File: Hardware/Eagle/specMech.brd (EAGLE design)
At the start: 142.2 x 121.9 mm, 86 parts, among them J1 PINHD-1X8-MOLEX-SHROUD, J2 JST-2-PIN-2B-PH-K-S(LF)(SN), J3 PINHD-1X8-MOLEX-SHROUD, J4 PINHD-1X8-MOLEX-SHROUD, J6 Molex 0022232081, J7 Lantronix XPORT, J8 Molex 0022232081, U1 MCP23008-E/SO, U10 ADS1115, U11 MCP23008-E/SO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

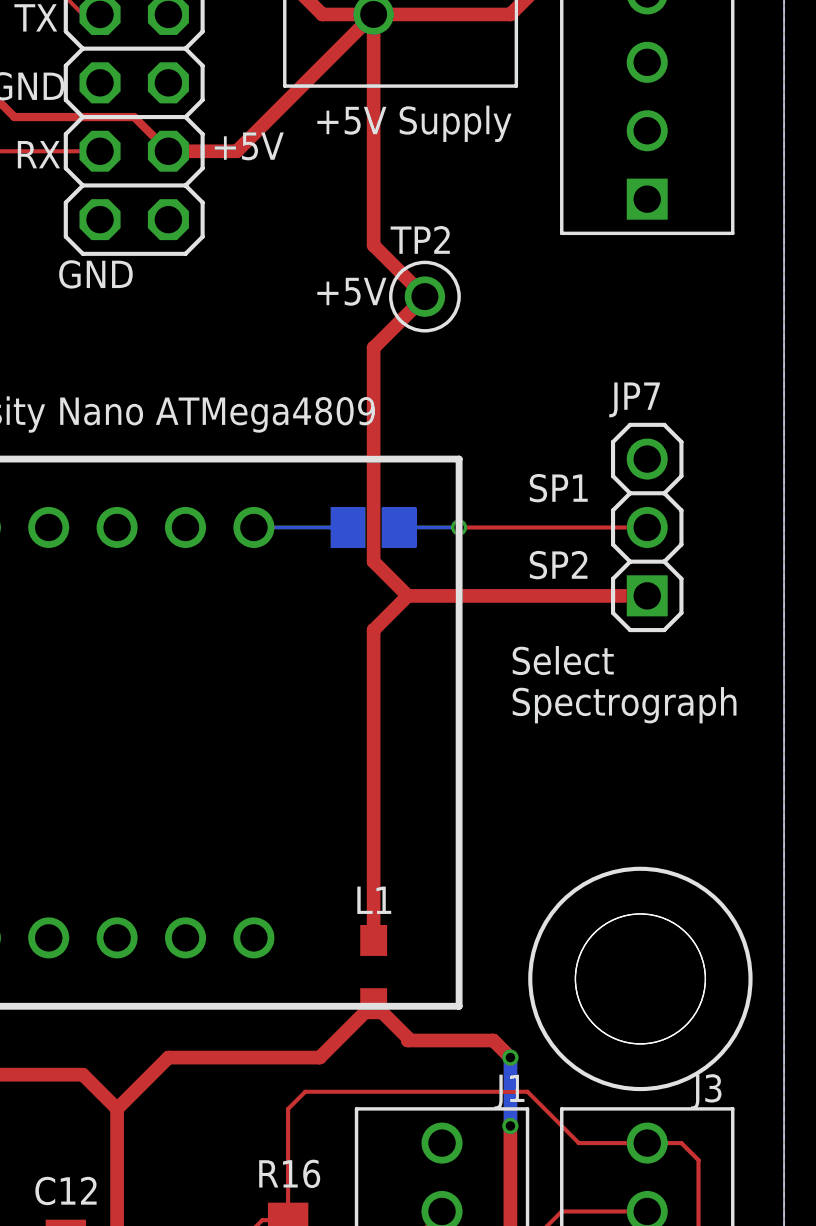
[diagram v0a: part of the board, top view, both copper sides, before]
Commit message: Starting major changes
Moved ferrite bead
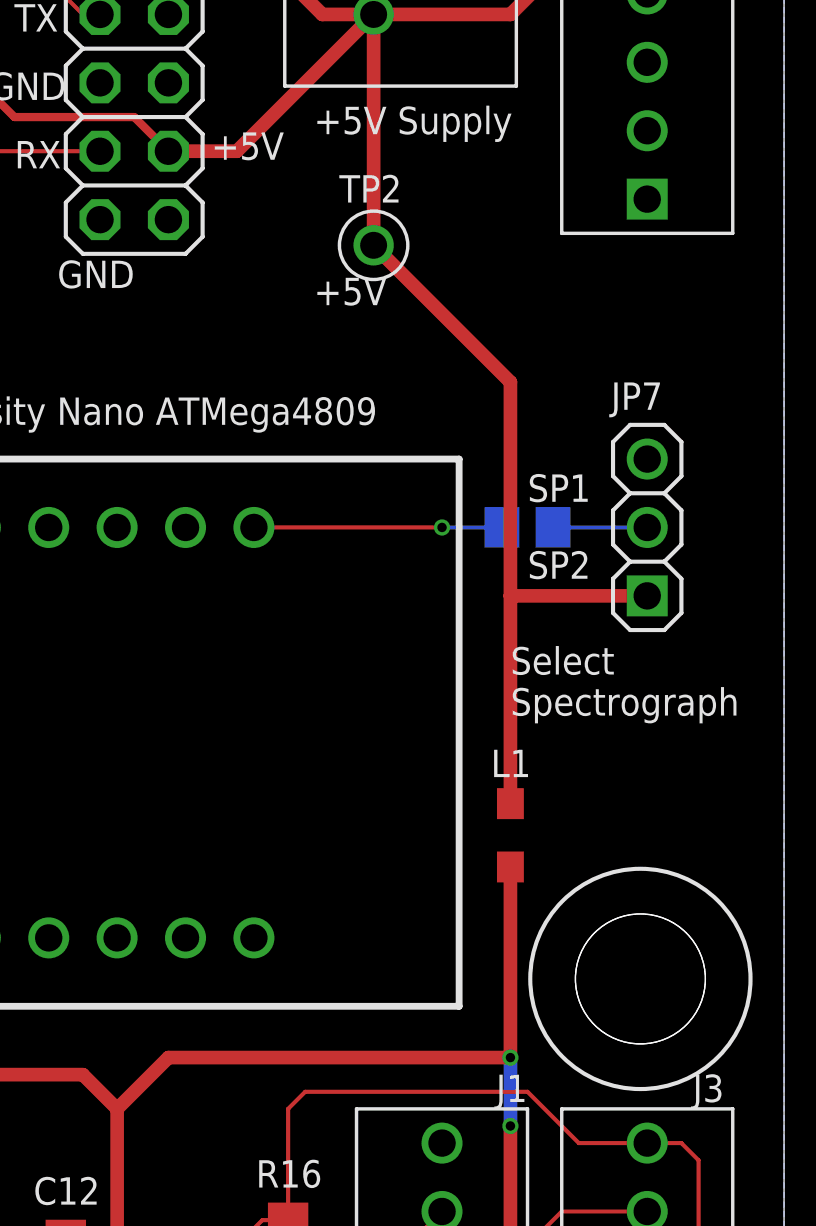
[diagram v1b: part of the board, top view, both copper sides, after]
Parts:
- moved L1 7.18 mm to (132.1, 55.9)
- moved R6 5.72 mm to (132.7, 67.3)
- moved TP2 2.69 mm to (127.0, 77.8)
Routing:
- net +5V: track 646.5 -> 637.1 mm
- net N$7: track 9.21 -> 3.50 mm, vias 1 -> 0
- net N$6: track 3.49 -> 9.21 mm, vias 0 -> 1
- net ADCVDD: track 132.5 -> 137.9 mm
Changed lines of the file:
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@@
 <attribute name="PURCHASE-URL" value="https://pricing.snapeda.com/search/part/EXB-38V103JV/?ref=eda" x="121.285" y="33.655" size="1.778" layer="27" display="off"/>
 </element>
-<element name="L1" library="AUmlib" library_urn="urn:adsk.eagle:library:9166017" package="INDC2012X87N" package3d_urn="urn:adsk.eagle:package:24287623/2" value="MMZ2012Y152BT000" x="127" y="50.8" smashed="yes" rot="R90">
-<attribute name="DESCRIPTION" value=" 1.5 kOhms @ 100MHz 1 Signal Line Ferrite Bead 0805 (2012 Metric) 500mA 400mOhm " x="127" y="50.8" size="1.778" layer="27" rot="R90" display="off"/>
-<attribute name="DIGI-KEY_PART_NUMBER" value="" x="127" y="50.8" size="1.778" layer="27" rot="R90" display="off"/>
-<attribute name="MF" value="TDK" x="127" y="50.8" size="1.778" layer="27" rot="R90" display="off"/>
-<attribute name="MP" value="MMZ2012Y152BT000" x="127" y="50.8" size="1.778" layer="27" rot="R90" display="off"/>
-<attribute name="NAME" x="127.768259375" y="53.975" size="1.016" layer="25" font="vector" rot="R180"/>
-<attribute name="PACKAGE" value="0805 TDK" x="127" y="50.8" size="1.778" layer="27" rot="R90" display="off"/>
-<attribute name="PURCHASE-URL" value="https://pricing.snapeda.com/search/part/MMZ2012Y152BT000/?ref=eda" x="127" y="50.8" size="1.778" layer="27" rot="R90" display="off"/>
+<element name="L1" library="AUmlib" library_urn="urn:adsk.eagle:library:9166017" package="INDC2012X87N" package3d_urn="urn:adsk.eagle:package:24287623/2" value="MMZ2012Y152BT000" x="132.08" y="55.88" smashed="yes" rot="R90">
+<attribute name="DESCRIPTION" value=" 1.5 kOhms @ 100MHz 1 Signal Line Ferrite Bead 0805 (2012 Metric) 500mA 400mOhm " x="132.08" y="55.88" size="1.778" layer="27" rot="R90" display="off"/>
+<attribute name="DIGI-KEY_PART_NUMBER" value="" x="132.08" y="55.88" size="1.778" layer="27" rot="R90" display="off"/>
+<attribute name="MF" value="TDK" x="132.08" y="55.88" size="1.778" layer="27" rot="R90" display="off"/>
+<attribute name="MP" value="MMZ2012Y152BT000" x="132.08" y="55.88" size="1.778" layer="27" rot="R90" display="off"/>
+<attribute name="NAME" x="132.848259375" y="59.055" size="1.016" layer="25" font="vector" rot="R180"/>
+<attribute name="PACKAGE" value="0805 TDK" x="132.08" y="55.88" size="1.778" layer="27" rot="R90" display="off"/>
+<attribute name="PURCHASE-URL" value="https://pricing.snapeda.com/search/part/MMZ2012Y152BT000/?ref=eda" x="132.08" y="55.88" size="1.778" layer="27" rot="R90" display="off"/>
 </element>
 <element name="C1" library="AUmlib" library_urn="urn:adsk.eagle:library:9166017" package="C0805" package3d_urn="urn:adsk.eagle:package:4021265/3" value="0.01uF" x="112.395" y="33.02" smashed="yes" rot="R270">
@@
 <attribute name="VALUE" x="140.335" y="63.5" size="1.27" layer="27" rot="R90"/>
 </element>
-<element name="R6" library="AUmlib" library_urn="urn:adsk.eagle:library:9166017" package="R0805" package3d_urn="urn:adsk.eagle:package:4021199/4" value="10K" x="127" y="67.31" smashed="yes" rot="MR180">
-<attribute name="NAME" x="126.365" y="69.85" size="1.016" layer="26" font="vector" rot="MR180"/>
-<attribute name="SPICEPREFIX" value="R" x="127" y="67.31" size="1.778" layer="28" rot="MR180" display="off"/>
-<attribute name="VALUE" x="125.095" y="69.85" size="1.016" layer="28" font="vector" rot="MR180"/>
+<element name="R6" library="AUmlib" library_urn="urn:adsk.eagle:library:9166017" package="R0805" package3d_urn="urn:adsk.eagle:package:4021199/4" value="10K" x="132.715" y="67.31" smashed="yes" rot="MR180">
+<attribute name="NAME" x="132.08" y="69.85" size="1.016" layer="26" font="vector" rot="MR180"/>
+<attribute name="SPICEPREFIX" value="R" x="132.715" y="67.31" size="1.778" layer="28" rot="MR180" display="off"/>
+<attribute name="VALUE" x="130.81" y="69.85" size="1.016" layer="28" font="vector" rot="MR180"/>
 </element>
 <element name="TP1" library="AUmlib" library_urn="urn:adsk.eagle:library:9166017" package="TP5000-TESTPOINT-BLK" package3d_urn="urn:adsk.eagle:package:24642442/4" value="TP5000-TESTPOINT-BLK" x="60.325" y="106.68" smashed="yes">
 <attribute name="NAME" x="59.055" y="108.2675" size="1.016" layer="25" font="vector"/>
 </element>
-<element name="TP2" library="AUmlib" library_urn="urn:adsk.eagle:library:9166017" package="TP5000-TESTPOINT-RED" package3d_urn="urn:adsk.eagle:package:24643663/2" value="TP5000-TESTPOINT-RED" x="128.905" y="75.8825" smashed="yes">
-<attribute name="NAME" x="127.635" y="77.47" size="1.016" layer="25" font="vector"/>
+<element name="TP2" library="AUmlib" library_urn="urn:adsk.eagle:library:9166017" package="TP5000-TESTPOINT-RED" package3d_urn="urn:adsk.eagle:package:24643663/2" value="TP5000-TESTPOINT-RED" x="127" y="77.7875" smashed="yes">
+<attribute name="NAME" x="125.73" y="79.375" size="1.016" layer="25" font="vector"/>
 </element>
 <element name="TP3" library="AUmlib" library_urn="urn:adsk.eagle:library:9166017" package="TP5000-TESTPOINT-BLU" package3d_urn="urn:adsk.eagle:package:24643711/2" value="TP5000-TESTPOINT-BLU" x="32.385" y="100.33" smashed="yes">
@@
 <wire x1="42.815" y1="44.18" x2="42.815" y2="44.0475" width="0.508" layer="1"/>
 <contactref element="JP7" pad="1"/>
-<wire x1="137.16" y1="64.77" x2="128.27" y2="64.77" width="0.508" layer="1"/>
-<wire x1="128.27" y1="64.77" x2="127" y2="63.5" width="0.508" layer="1"/>
-<wire x1="127" y1="63.5" x2="127" y2="51.975" width="0.508" layer="1"/>
-<wire x1="128.27" y1="64.77" x2="127" y2="66.04" width="0.508" layer="1"/>
+<wire x1="137.16" y1="64.77" x2="132.08" y2="64.77" width="0.508" layer="1"/>
 <contactref element="TP2" pad="P$1"/>
 <wire x1="127" y1="86.36" x2="127" y2="77.7875" width="0.508" layer="1"/>
-<wire x1="127" y1="77.7875" x2="128.905" y2="75.8825" width="0.508" layer="1"/>
-<wire x1="127" y1="66.04" x2="127" y2="73.9775" width="0.508" layer="1"/>
-<wire x1="127" y1="73.9775" x2="128.905" y2="75.8825" width="0.508" layer="1"/>
+<wire x1="132.08" y1="72.7075" x2="127" y2="77.7875" width="0.508" layer="1"/>
+<wire x1="132.08" y1="72.7075" x2="132.08" y2="64.77" width="0.508" layer="1"/>
+<wire x1="132.08" y1="57.055" x2="132.08" y2="64.77" width="0.508" layer="1"/>
 </signal>
 <signal name="XP-TX">
@@
 <wire x1="108.27" y1="21.27" x2="111.125" y2="18.415" width="0.1524" layer="1"/>
 <wire x1="111.125" y1="18.415" x2="112.6396" y2="18.415" width="0.1524" layer="1"/>
-<wire x1="127" y1="49.625" x2="128.27" y2="48.355" width="0.508" layer="1"/>
-<wire x1="128.27" y1="48.355" x2="128.27" y2="48.26" width="0.508" layer="1"/>
-<wire x1="128.27" y1="48.26" x2="131.445" y2="48.26" width="0.508" layer="1"/>
-<wire x1="131.445" y1="48.26" x2="132.08" y2="47.625" width="0.508" layer="1"/>
 <contactref element="U11" pad="18"/>
 <contactref element="C21" pad="1"/>
@@
 <wire x1="95.25" y1="46.355" x2="95.885" y2="46.99" width="0.508" layer="16"/>
 <via x="95.885" y="46.99" extent="1-16" drill="0.35"/>
-<wire x1="125" y1="47.625" x2="119.38" y2="47.625" width="0.508" layer="1"/>
 <wire x1="119.38" y1="47.625" x2="117.475" y2="45.72" width="0.508" layer="1"/>
 <wire x1="117.475" y1="45.72" x2="117.475" y2="40.005" width="0.508" layer="1"/>
 <wire x1="117.475" y1="40.005" x2="116.525" y2="39.055" width="0.508" layer="1"/>
 <wire x1="116.525" y1="39.055" x2="115.57" y2="39.055" width="0.508" layer="1"/>
-<wire x1="127" y1="49.625" x2="125" y2="47.625" width="0.508" layer="1"/>
 <wire x1="95.885" y1="46.99" x2="116.205" y2="46.99" width="0.508" layer="1"/>
 <wire x1="116.205" y1="46.99" x2="117.475" y2="45.72" width="0.508" layer="1"/>
@@
 <wire x1="112.6396" y1="18.415" x2="115.89" y2="18.415" width="0.254" layer="1"/>
 <wire x1="115.89" y1="18.415" x2="116.205" y2="18.1" width="0.254" layer="1"/>
+<wire x1="132.08" y1="54.705" x2="132.08" y2="47.625" width="0.508" layer="1"/>
+<wire x1="132.08" y1="47.625" x2="119.38" y2="47.625" width="0.508" layer="1"/>
 </signal>
 <signal name="RC-TX">
@@
 <contactref element="CNANO1" pad="PF2"/>
 <contactref element="R6" pad="1"/>
-<wire x1="122.555" y1="67.31" x2="126.05" y2="67.31" width="0.1524" layer="16"/>
+<wire x1="131.765" y1="67.31" x2="129.54" y2="67.31" width="0.1524" layer="16"/>
+<via x="129.54" y="67.31" extent="1-16" drill="0.35"/>
+<wire x1="129.54" y1="67.31" x2="122.555" y2="67.31" width="0.1524" layer="1"/>
 </signal>
 <signal name="N$7">
 <contactref element="R6" pad="2"/>
 <contactref element="JP7" pad="2"/>
-<wire x1="127.95" y1="67.31" x2="130.175" y2="67.31" width="0.1524" layer="16"/>
-<via x="130.175" y="67.31" extent="1-16" drill="0.35"/>
-<wire x1="130.175" y1="67.31" x2="137.16" y2="67.31" width="0.1524" layer="1"/>
+<wire x1="133.665" y1="67.31" x2="137.16" y2="67.31" width="0.1524" layer="16"/>
 </signal>
 <signal name="A0B">

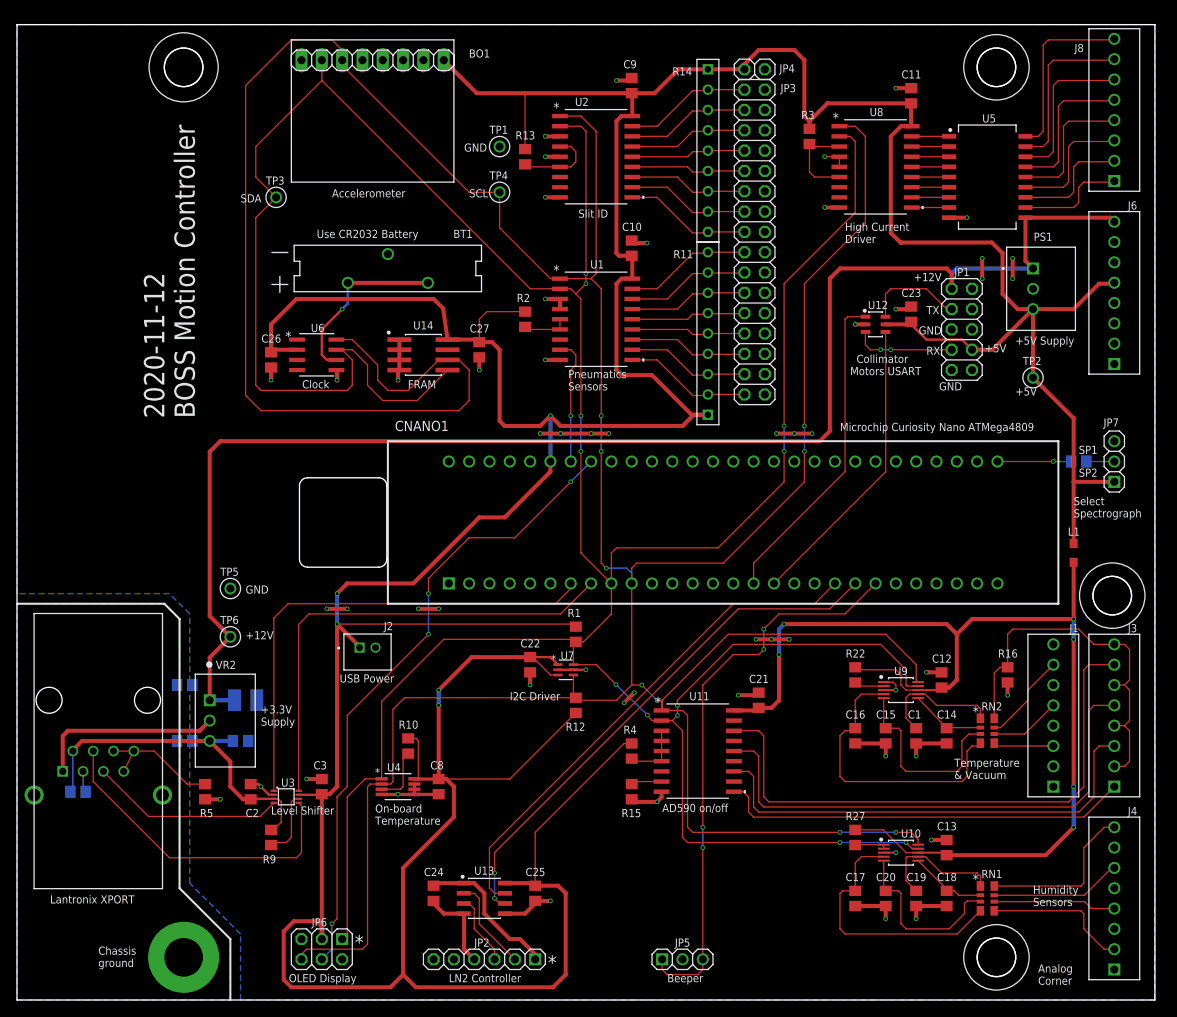
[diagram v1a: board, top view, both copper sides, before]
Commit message: Swapped castellated board in, starting rerouting
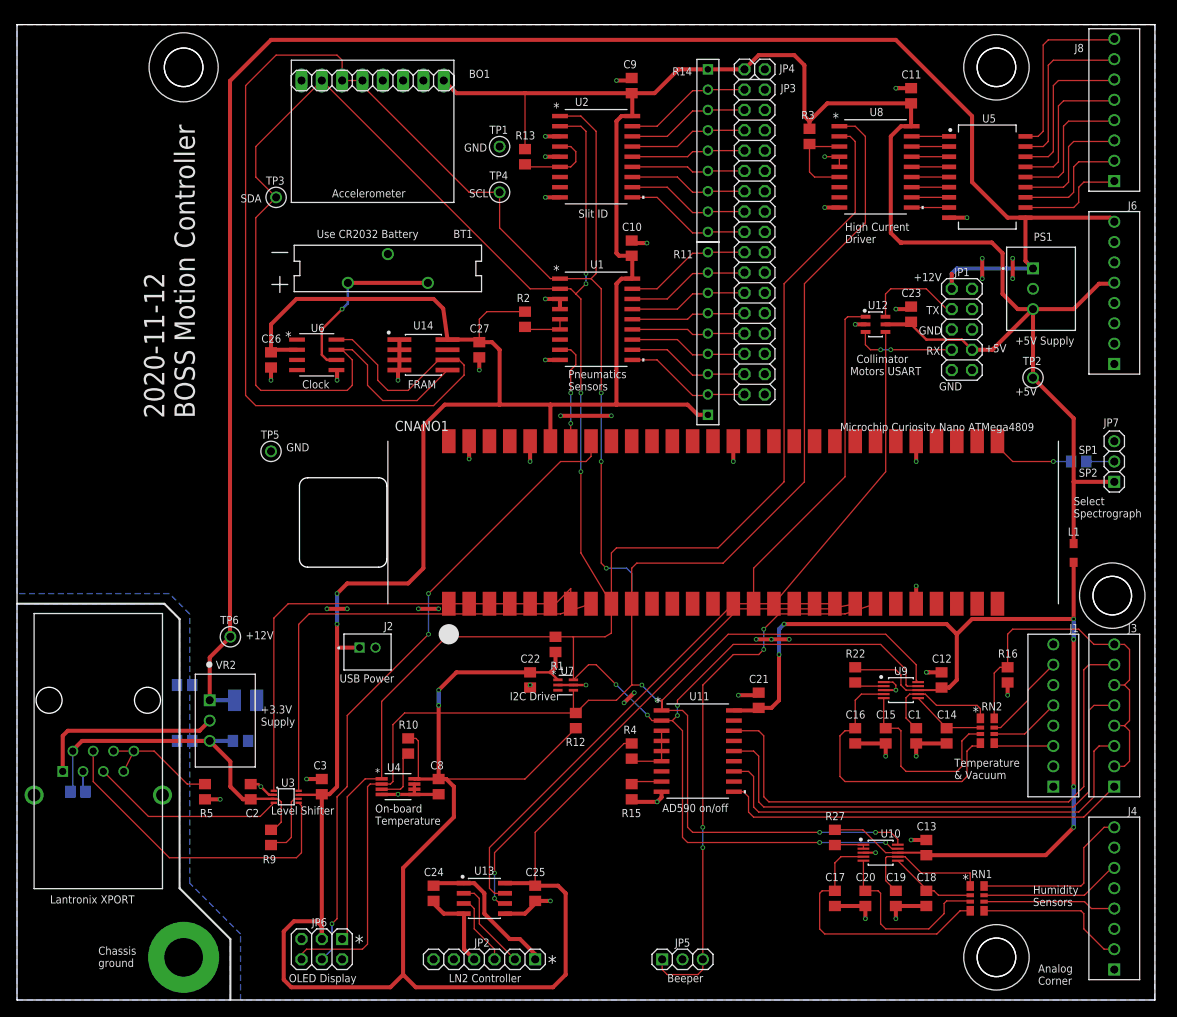
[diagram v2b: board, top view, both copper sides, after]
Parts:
- CNANO1: value CURIOSITYNANO4809 -> CURIOSITYNANO4809CASTELLATED; device AUmlib:CURIOSITYNANO4809 -> AUmlib:CURIOSITYNANO4809CASTELLATED
- moved TP5 17.9 mm to (31.8, 68.6)
- moved R1 2.84 mm to (67.3, 44.5), turned to 270 degrees
- moved BO1 2.54 mm to (44.5, 108.6)
- moved C17 2.54 mm to (102.2, 12.7)
- moved R27 2.54 mm to (102.2, 20.3)
- moved C13 2.54 mm to (113.7, 19.1)
- moved C18 2.54 mm to (113.7, 12.7)
- moved C19 2.54 mm to (109.9, 12.7)
- moved C20 2.54 mm to (106.0, 12.7)
- moved U10 2.54 mm to (108.0, 18.4)
- moved R12 1.91 mm to (69.8, 34.9)
- moved U7 1.91 mm to (68.6, 39.4)
- moved C22 1.90 mm to (64.1, 40.0)
- moved RN1 1.27 mm to (120.0, 12.7)
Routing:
- net +12V: track 182.3 -> 229.5 mm
- net +5V: track 637.1 -> 593.1 mm, vias 5 -> 4
- net SCL: track 481.9 -> 476.0 mm, vias 9 -> 7
- net GND: track 156.4 -> 160.5 mm
- net ADCVDD: track 137.9 -> 140.4 mm
- net RC-RX: track 40.5 -> 43.0 mm
- net INT-PNEU: track 15.8 -> 13.3 mm, vias 1 -> 2
- net RC-TX: track 37.2 -> 39.1 mm
- net N$65: track 16.2 -> 17.7 mm
- net N$6: track 9.21 -> 10.6 mm
- net RX: track 59.5 -> 58.1 mm
- net BEEP: track 70.8 -> 69.4 mm
- net TX: track 60.9 -> 62.1 mm
- net N$68: track 22.1 -> 23.4 mm
- net A1B: track 15.4 -> 16.6 mm
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
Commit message: More routing
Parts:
- moved R12 11.5 mm to (77.5, 43.5)
- moved RN1 9.67 mm to (111.1, 8.89)
- moved C13 8.83 mm to (106.7, 13.7)
- moved C17 8.83 mm to (95.2, 7.30)
- moved C18 8.83 mm to (106.7, 7.30)
- moved C19 8.83 mm to (102.9, 7.30)
- moved C20 8.83 mm to (99.1, 7.30)
- moved R27 8.83 mm to (95.2, 14.9)
- moved U10 8.83 mm to (101.0, 13.0)
- moved C21 8.57 mm to (92.7, 28.9)
- moved R15 8.57 mm to (76.8, 17.5)
- moved R4 8.57 mm to (76.8, 22.5)
- moved U11 8.57 mm to (85.1, 22.5)
- moved R1 6.42 mm to (73.7, 43.5)
- moved C22 5.28 mm to (68.6, 37.1)
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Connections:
- new net N$27: J1.P$2
- net A0B: now also J4.P$1; no longer J4.P$2
- net A1B: now also J4.P$3; no longer J4.P$4
- net A2B: now also J4.P$5; no longer J4.P$6
- net A3B: now also J4.P$7; no longer J4.P$8
- net GND: now also J4.P$2, J4.P$4, J4.P$6, J4.P$8; no longer J4.P$1, J4.P$3, J4.P$5, J4.P$7
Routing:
- net ADCVDD: track 140.4 -> 158.4 mm
- net A0B: track 19.4 -> 33.2 mm
- net A1B: track 16.6 -> 28.6 mm
- net LN-TX: track 65.1 -> 76.5 mm
- net LN-RX: track 63.1 -> 73.9 mm
- net A2B: track 17.7 -> 27.9 mm
- net A3B: track 21.9 -> 32.1 mm
- net SDA: track 440.0 -> 431.6 mm
- net N$72: track 71.4 -> 64.0 mm
- net +5V: track 593.1 -> 586.1 mm
- net A2A: track 11.4 -> 16.9 mm
- net N$71: track 65.0 -> 60.3 mm
- net N$65: track 17.7 -> 14.2 mm
- net A1A: track 8.87 -> 12.3 mm
- net N$62: track 37.0 -> 33.6 mm
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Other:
- board text added: "Temperature & Humidity"
- board text added: "Vacuum"
- board text removed: "Humidity Sensors"
- board text removed: "Temperature & Vacuum"

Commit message: More routing, mostly OK now
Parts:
- moved TP1 2.62 mm to (59.7, 109.2)
- moved L1 0.95 mm to (132.1, 56.8)
- moved TP4 0.64 mm to (59.7, 101.0)
- moved R6 0.32 mm to (133.0, 67.3)
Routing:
- net LN-RX: track 73.9 -> 62.8 mm
- net LN-TX: track 76.5 -> 65.7 mm
- net ADCVDD: track 158.4 -> 154.5 mm, vias 6 -> 4
- net +5V: track 586.1 -> 589.5 mm
- net GND: track 162.5 -> 160.0 mm, vias 54 -> 52
- net SDA: track 431.6 -> 430.4 mm
- net N$69: track 35.5 -> 34.5 mm
- net SCL: track 475.2 -> 476.0 mm
- net N$68: track 24.0 -> 23.4 mm
- net A3A: vias 0 -> 2
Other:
- board text added: "2021-01-26 BOSS Motion Controller"
- board text removed: "2020-11-12 BOSS Motion Controller"
